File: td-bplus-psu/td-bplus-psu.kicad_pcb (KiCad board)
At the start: 2 copper layers, 40 x 40 mm, 23 parts, among them J1 Conn_01x08_Pin, Q13 BSZ42DN25NS3GATMA1, U14 LT3758AEMSE

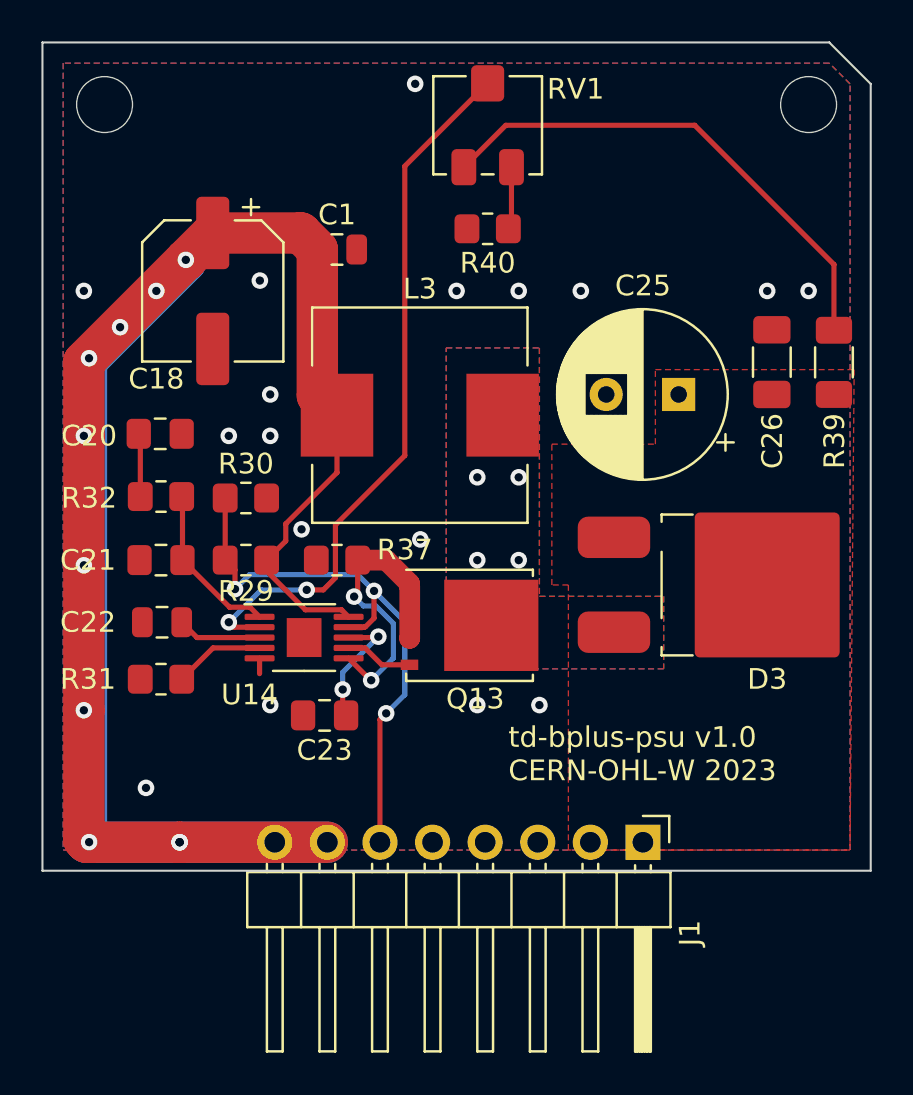
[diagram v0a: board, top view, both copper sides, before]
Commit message: Update bplus psu to have better caps and pot facing the right dir
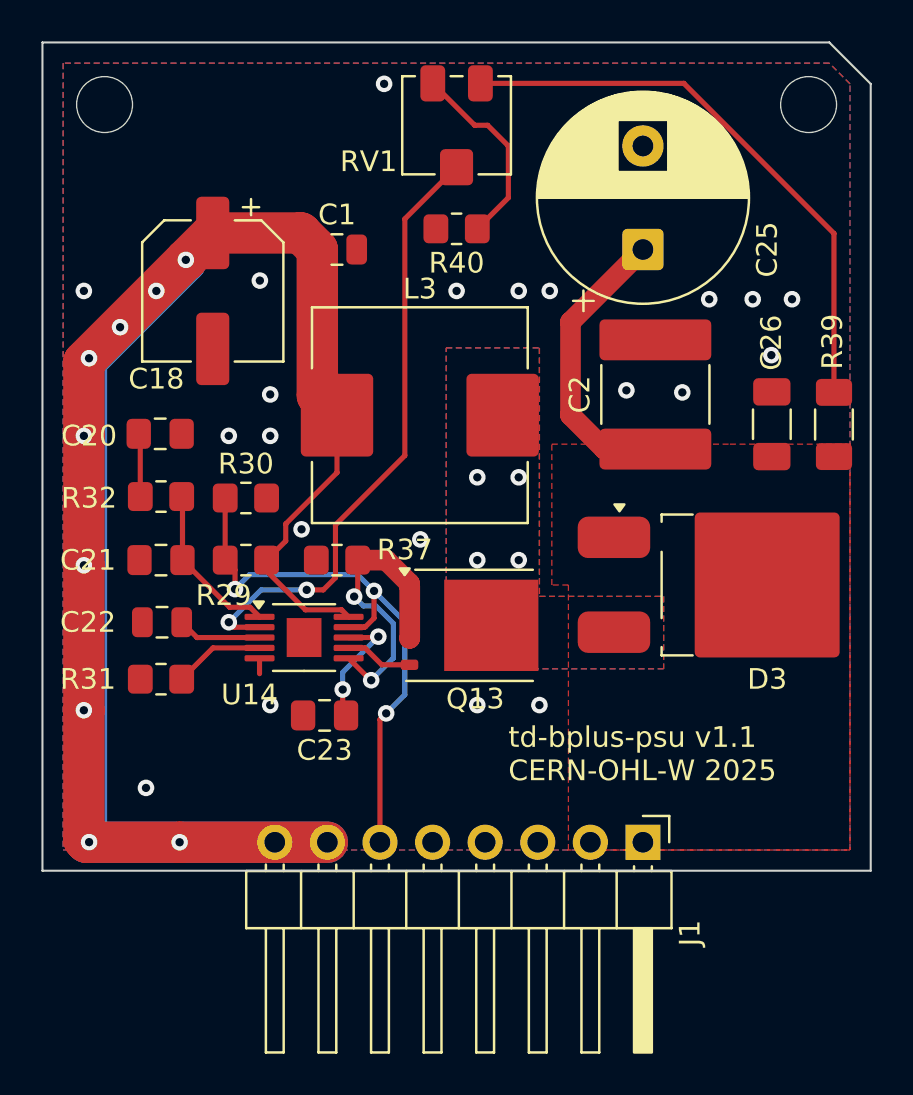
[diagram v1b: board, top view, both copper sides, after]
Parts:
- added C2: 1uF, Capacitor_SMD:C_2220_5750Metric_Pad1.97x5.40mm_HandSolder, F.Cu at (146.6, 105.0)
- C25: value 10uF -> 8.2uF; footprint Capacitor_THT:CP_Radial_D8.0mm_P3.50mm -> Capacitor_THT:CP_Radial_D10.0mm_P5.00mm
- Q13: value BSZ42DN25NS3GATMA1 -> ~
- moved C25 7.21 mm to (146.0, 98.0), turned to 90 degrees
- moved C26 3.00 mm to (152.2, 106.4)
- moved R39 3.00 mm to (155.2, 106.5)
- moved R40 1.50 mm to (137.0, 97.0)
- moved RV1 1.50 mm to (137.0, 92.0), turned to 0 degrees
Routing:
- net HT: track 0.00 -> 14.2 mm
- net Net-(R40-Pad1): track 3.04 -> 9.52 mm
- net Net-(U14-FBX): track 34.5 -> 29.9 mm
- net Net-(R39-Pad2): track 24.7 -> 27.8 mm
- net GND: vias 17 -> 21
- net +48V: vias 10 -> 9
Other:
- board text added: "td-bplus-psu v1.1 CERN-OHL-W 2025"
- board text removed: "td-bplus-psu v1.0 CERN-OHL-W 2023"
